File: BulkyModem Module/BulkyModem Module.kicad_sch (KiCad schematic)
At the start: 13 parts, among them M1 Mounting, M2 Mounting, M3 Mounting, M4 Mounting, SW1 SET_1200, U1 74HCT244, U6 74HCT32

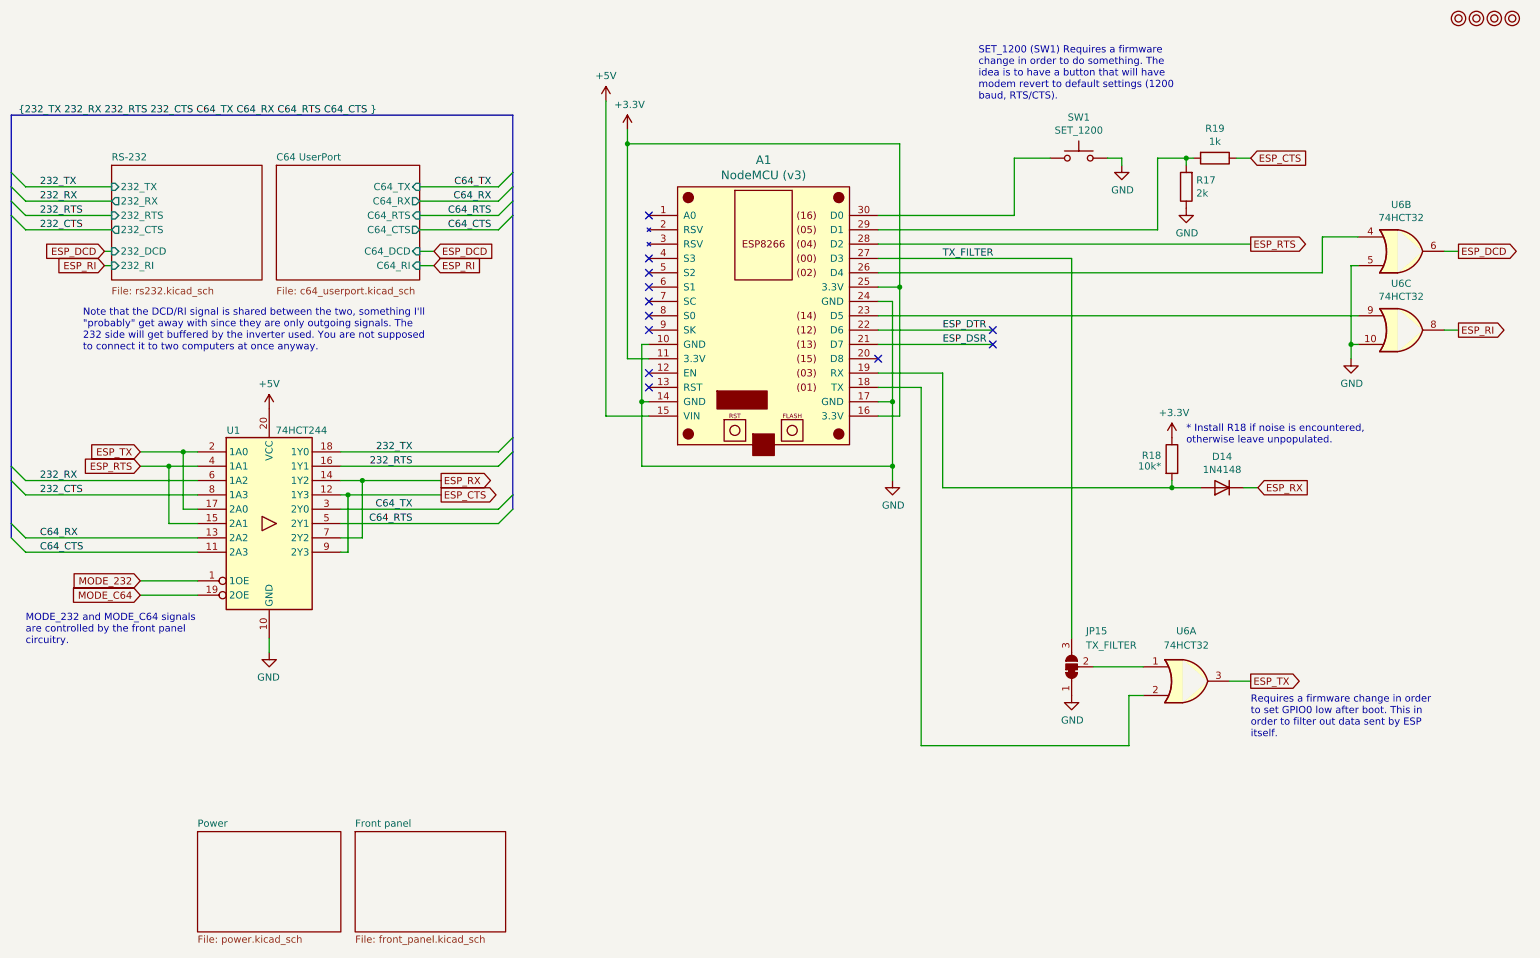
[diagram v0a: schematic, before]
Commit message: Add mounting points for audio module
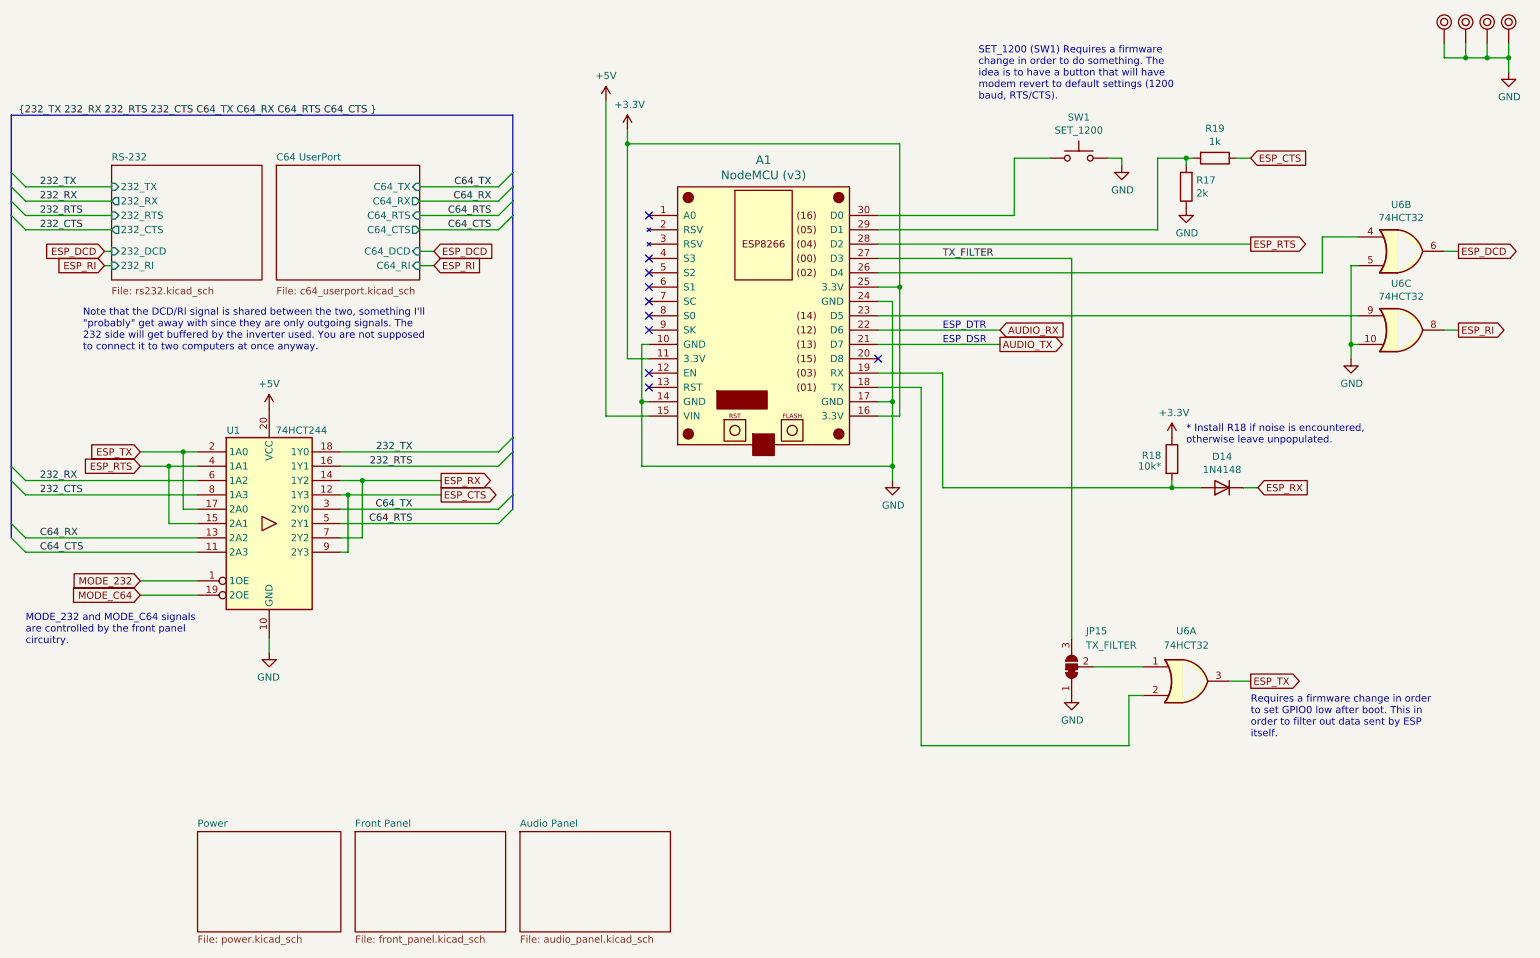
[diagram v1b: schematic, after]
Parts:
- M1, M2, M3, M4: footprint mounting:M3 -> mounting:M3_pin; symbol mounting:Mounting -> mounting:Mounting_Pin
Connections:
- net GND: now also M1.1, M2.1, M3.1, M4.1
- net ESP_DSR renamed AUDIO_TX
- net ESP_DTR renamed AUDIO_RX
- no-connect marks 12 -> 10
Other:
- sheet Front panel renamed Front Panel
- added sheet Audio Panel (audio_panel.kicad_sch)
- note added: "ESP_DSR"
- note added: "ESP_DTR"

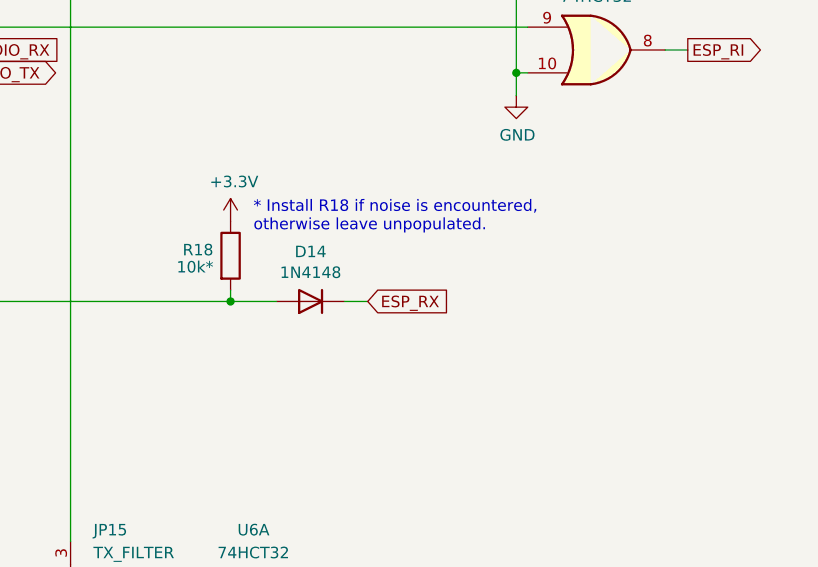
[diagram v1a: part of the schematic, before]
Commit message: Add labels to LEDs
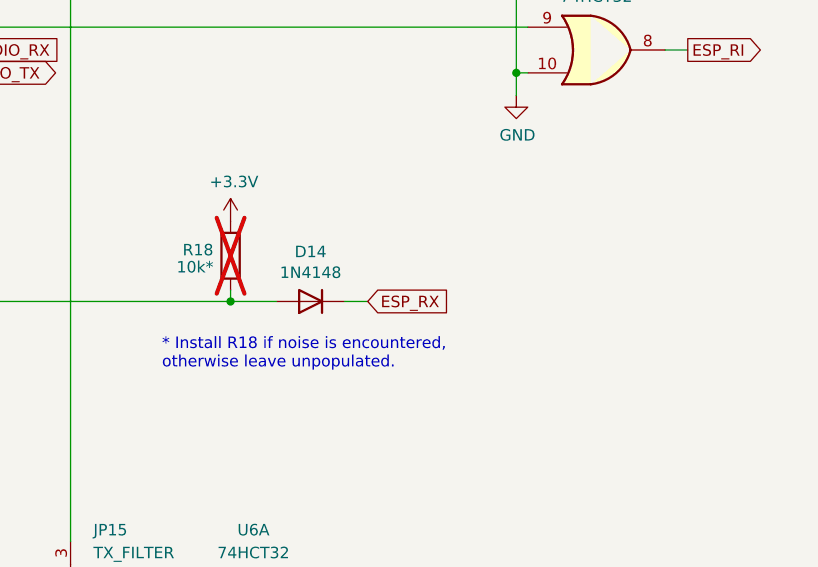
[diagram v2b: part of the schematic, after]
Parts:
- R18: now not fitted
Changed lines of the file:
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@@
 	(text "* Install R18 if noise is encountered,\notherwise leave unpopulated."
 		(exclude_from_sim no)
-		(at 224.79 90.17 0)
+		(at 214.63 105.41 0)
 		(effects
 			(font
@@
 		(in_bom yes)
 		(on_board yes)
-		(dnp no)
+		(dnp yes)
 		(property "Reference" "R18"
 			(at 220.345 92.075 0)
